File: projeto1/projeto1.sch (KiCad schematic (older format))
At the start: 4 parts

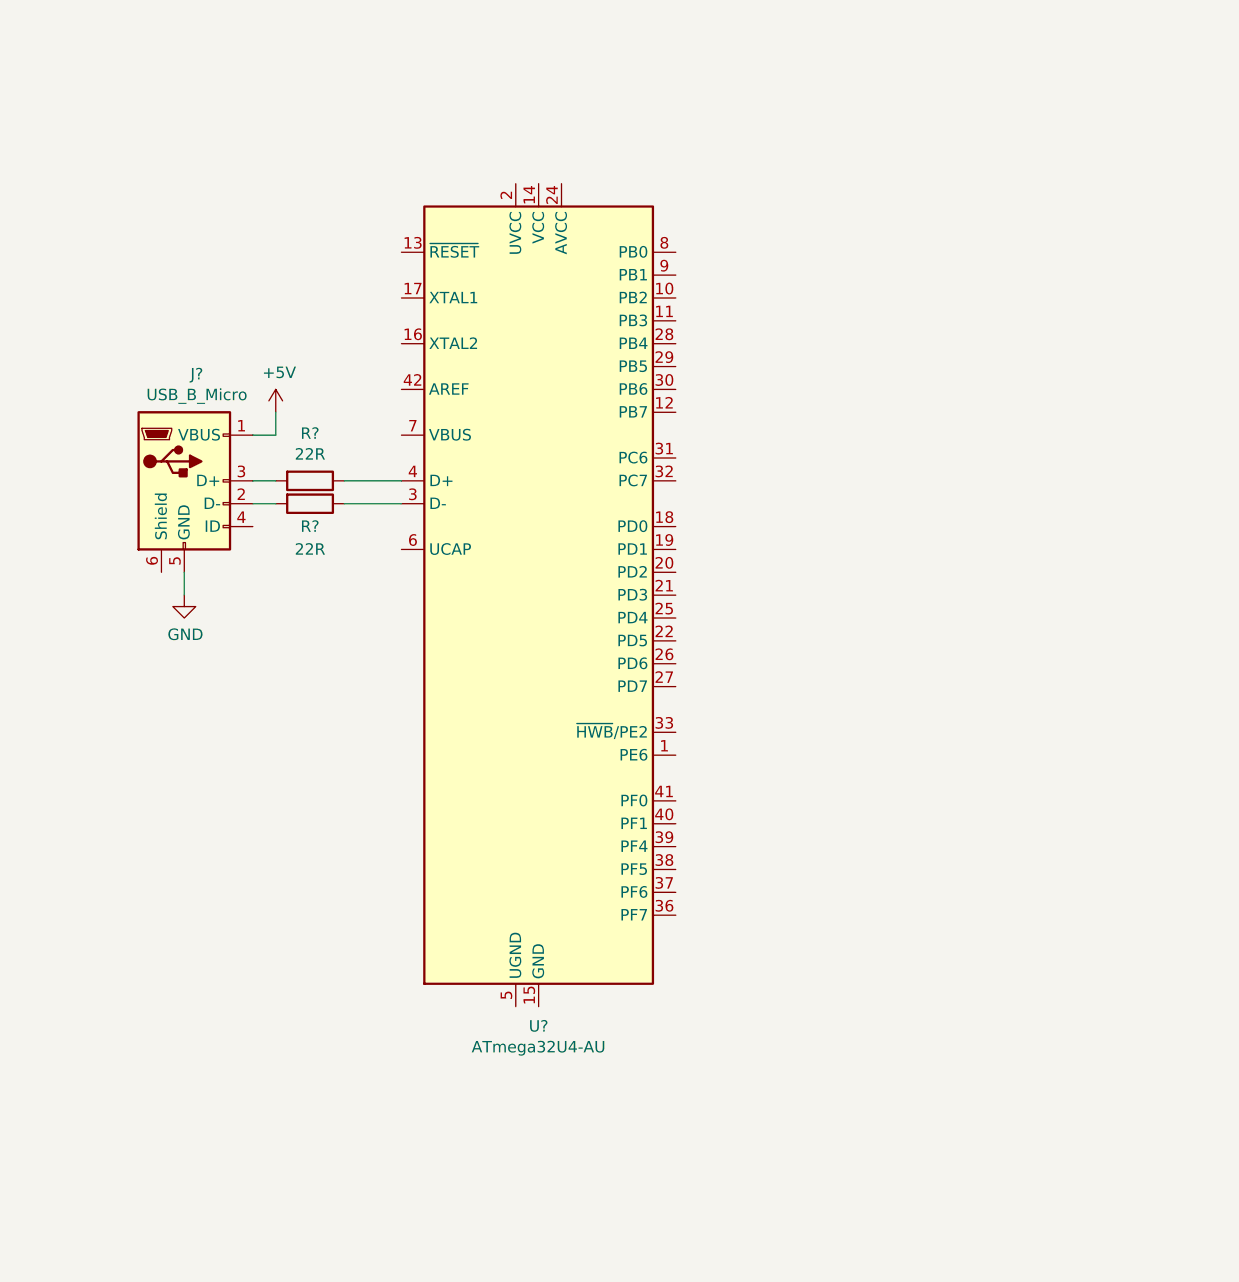
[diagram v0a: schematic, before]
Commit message: Crystal, Capacitores de Bypass e UCAP adicionados
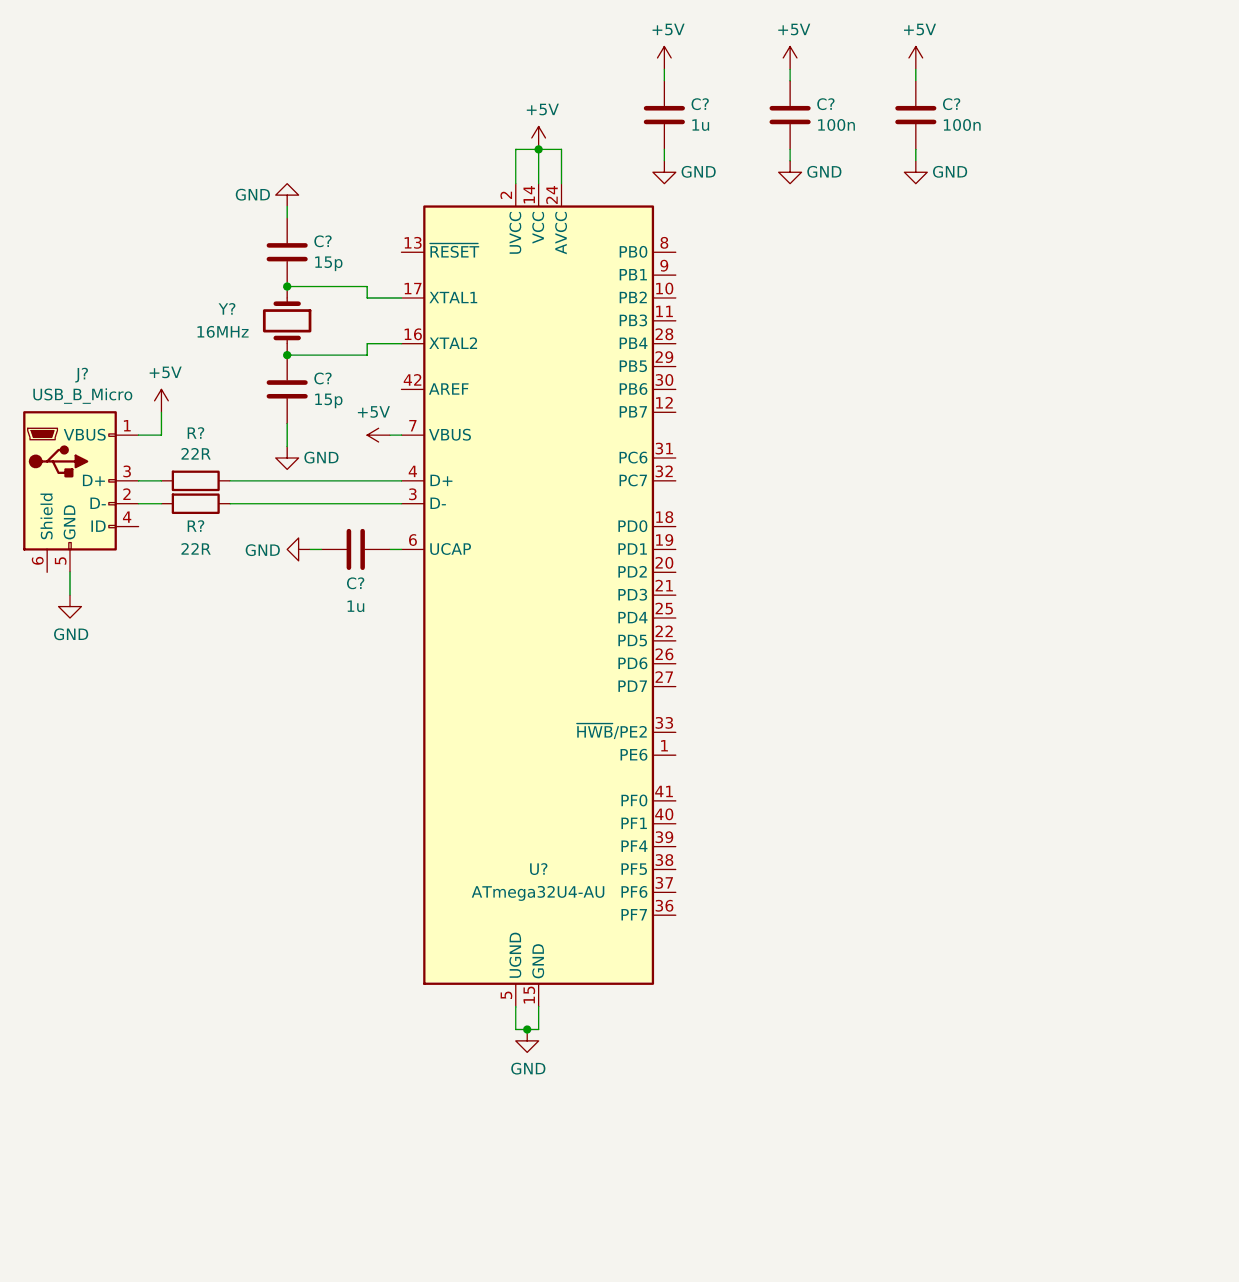
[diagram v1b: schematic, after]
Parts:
- added C? (x2): 15p, symbol Device:C
- added C? (x2): 1u, symbol Device:C
- added C? (x2): 100n, symbol Device:C
- added Y?: 16MHz, symbol Device:Crystal
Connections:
- net +5V: now also U?.14 (VCC), U?.2 (UVCC), U?.24 (AVCC), U?.34 (VCC), U?.44 (AVCC), U?.7 (VBUS), C?.1, C?.1, C?.1
- net GND: now also U?.15 (GND), U?.23 (GND), U?.35 (GND), U?.43 (GND), U?.5 (UGND), C?.1, C?.2, C?.2, C?.2, C?.2, C?.2
- net at U?.16 (XTAL2): now also C?.1, Y?.2
- net at U?.17 (XTAL1): now also C?.2, Y?.1
- net at U?.6 (UCAP): now also C?.1
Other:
- moved on the sheet: J?, R?

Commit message: Reset e Pin Headers adicionados
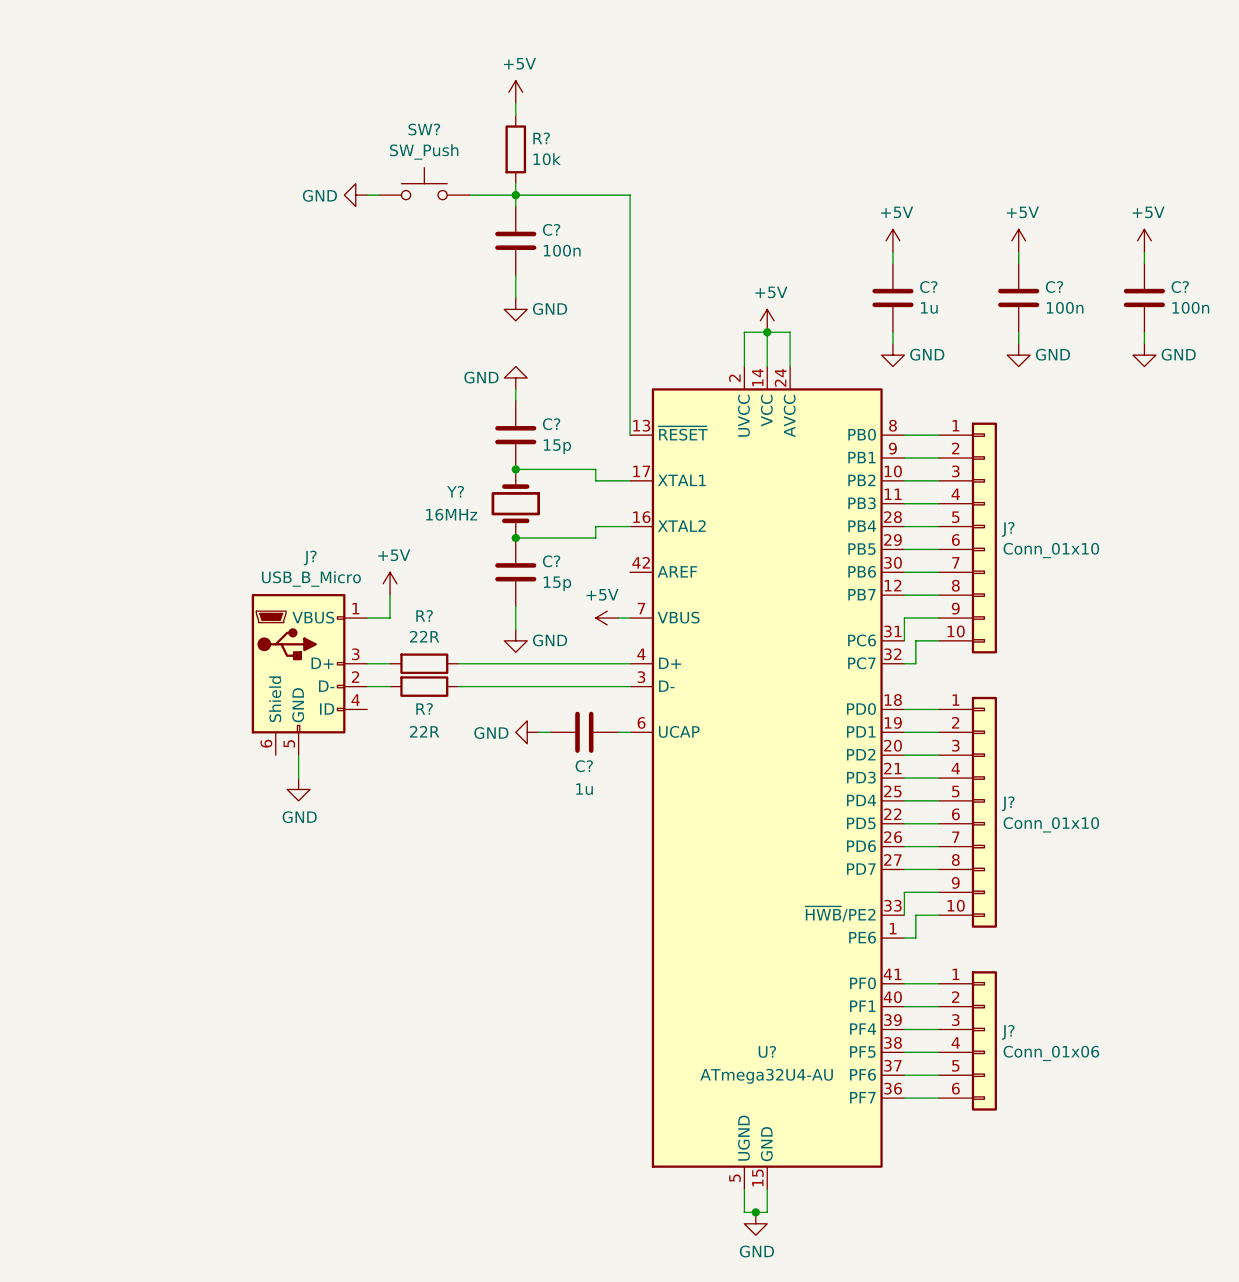
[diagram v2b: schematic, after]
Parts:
- added C?: 100n, symbol Device:C
- added J? (x2): Conn_01x10, symbol Connector_Generic:Conn_01x10
- added J?: Conn_01x06, symbol Connector_Generic:Conn_01x06
- added R?: 10k, symbol Device:R
- added SW?: SW_Push, symbol Switch:SW_Push
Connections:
- net +5V: now also R?.1
- net GND: now also C?.2, SW?.1
- net at U?.1 (PE6): now also J?.10 (Pin_10)
- net at U?.10 (PB2): now also J?.3 (Pin_3)
- net at U?.11 (PB3): now also J?.4 (Pin_4)
- net at U?.12 (PB7): now also J?.8 (Pin_8)
- net at U?.13 (~RESET): now also C?.1, R?.2, SW?.2
- net at U?.18 (PD0): now also J?.1 (Pin_1)
- net at U?.19 (PD1): now also J?.2 (Pin_2)
- net at U?.20 (PD2): now also J?.3 (Pin_3)
- net at U?.21 (PD3): now also J?.4 (Pin_4)
- net at U?.22 (PD5): now also J?.6 (Pin_6)
- net at U?.25 (PD4): now also J?.5 (Pin_5)
- net at U?.26 (PD6): now also J?.7 (Pin_7)
- net at U?.27 (PD7): now also J?.8 (Pin_8)
- net at U?.28 (PB4): now also J?.5 (Pin_5)
- net at U?.29 (PB5): now also J?.6 (Pin_6)
- net at U?.30 (PB6): now also J?.7 (Pin_7)
- net at U?.31 (PC6): now also J?.9 (Pin_9)
- net at U?.32 (PC7): now also J?.10 (Pin_10)
- net at U?.33 (~HWB~/PE2): now also J?.9 (Pin_9)
- net at U?.36 (PF7): now also J?.6 (Pin_6)
- net at U?.37 (PF6): now also J?.5 (Pin_5)
- net at U?.38 (PF5): now also J?.4 (Pin_4)
- net at U?.39 (PF4): now also J?.3 (Pin_3)
- net at U?.40 (PF1): now also J?.2 (Pin_2)
- net at U?.41 (PF0): now also J?.1 (Pin_1)
- net at U?.8 (PB0): now also J?.1 (Pin_1)
- net at U?.9 (PB1): now also J?.2 (Pin_2)
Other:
- moved on the sheet: C?, J?, R?, U?, Y?
